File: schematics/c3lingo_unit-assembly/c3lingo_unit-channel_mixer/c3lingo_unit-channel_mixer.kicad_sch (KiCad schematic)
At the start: 83 parts, among them J301 Interconnect, J302 PowerSupply, J303 Output, J304 Inputs, SW301 OnAir_X, SW302 Mute_X, U301 LM833N, U302 LM339, U303 LM339, U304 LM339, U305 LM833N

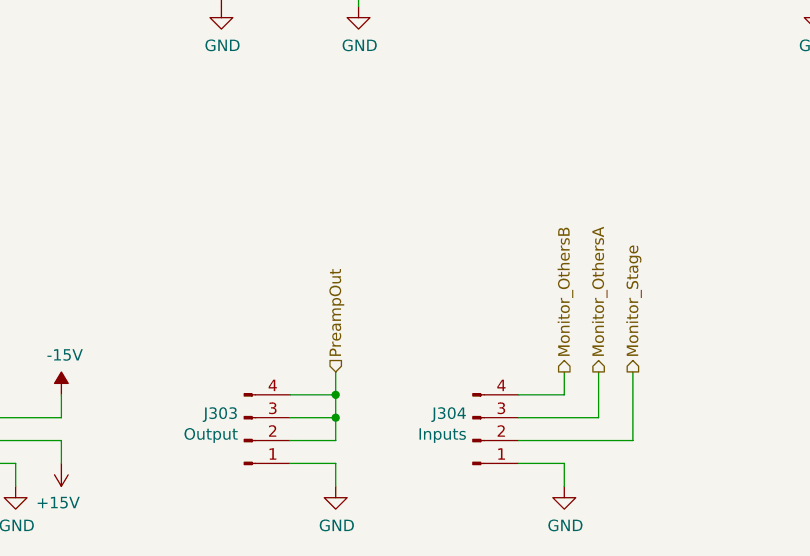
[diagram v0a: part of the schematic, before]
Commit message: Reworks board-to-board connections
Instead of having connections between all boards, use the mix_io board as an audio signal distribution hub.

Note: PCB not updated
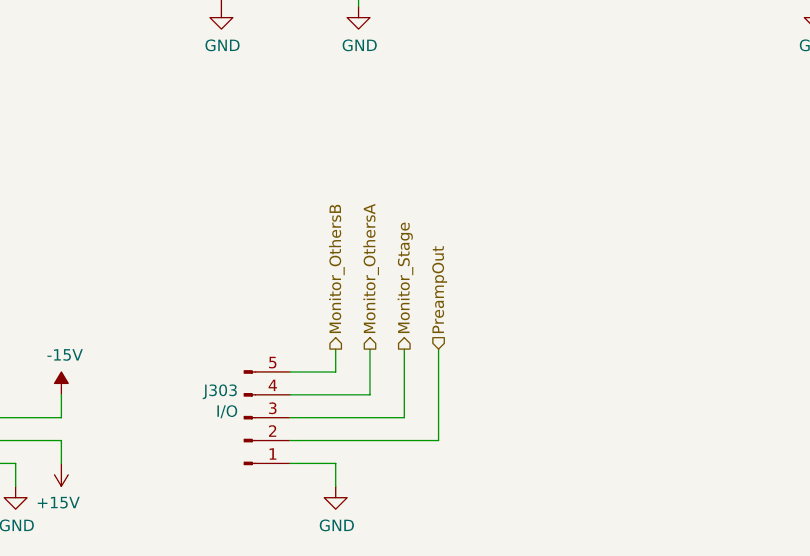
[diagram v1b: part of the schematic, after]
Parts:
- removed J304: Inputs, TerminalBlock_Phoenix:TerminalBlock_Phoenix_PTSM-0,5-4-2.5-H-THR_1x04_P2.50mm_Horizontal, symbol Connector:Conn_01x04_Pin
- J303: value Output -> I/O; footprint TerminalBlock_Phoenix:TerminalBlock_Phoenix_PTSM-0,5-4-2.5-H-THR_1x04_P2.50mm_Horizontal -> TerminalBlock_Phoenix:TerminalBlock_Phoenix_PTSM-0,5-5-2.5-H-THR_1x05_P2.50mm_Horizontal; symbol Connector:Conn_01x04_Pin -> Connector:Conn_01x05_Pin; Model PTSM 0,5/ 4-2,5-H THR -> PTSM 0,5/ 5-2,5-H THR
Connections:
- net Monitor_OthersA: now also J303.4 (Pin_4)
- net Monitor_OthersB: now also J303.5 (Pin_5)
- net Monitor_Stage: now also J303.3 (Pin_3)
- net PreampOut: no longer J303.3 (Pin_3), J303.4 (Pin_4)

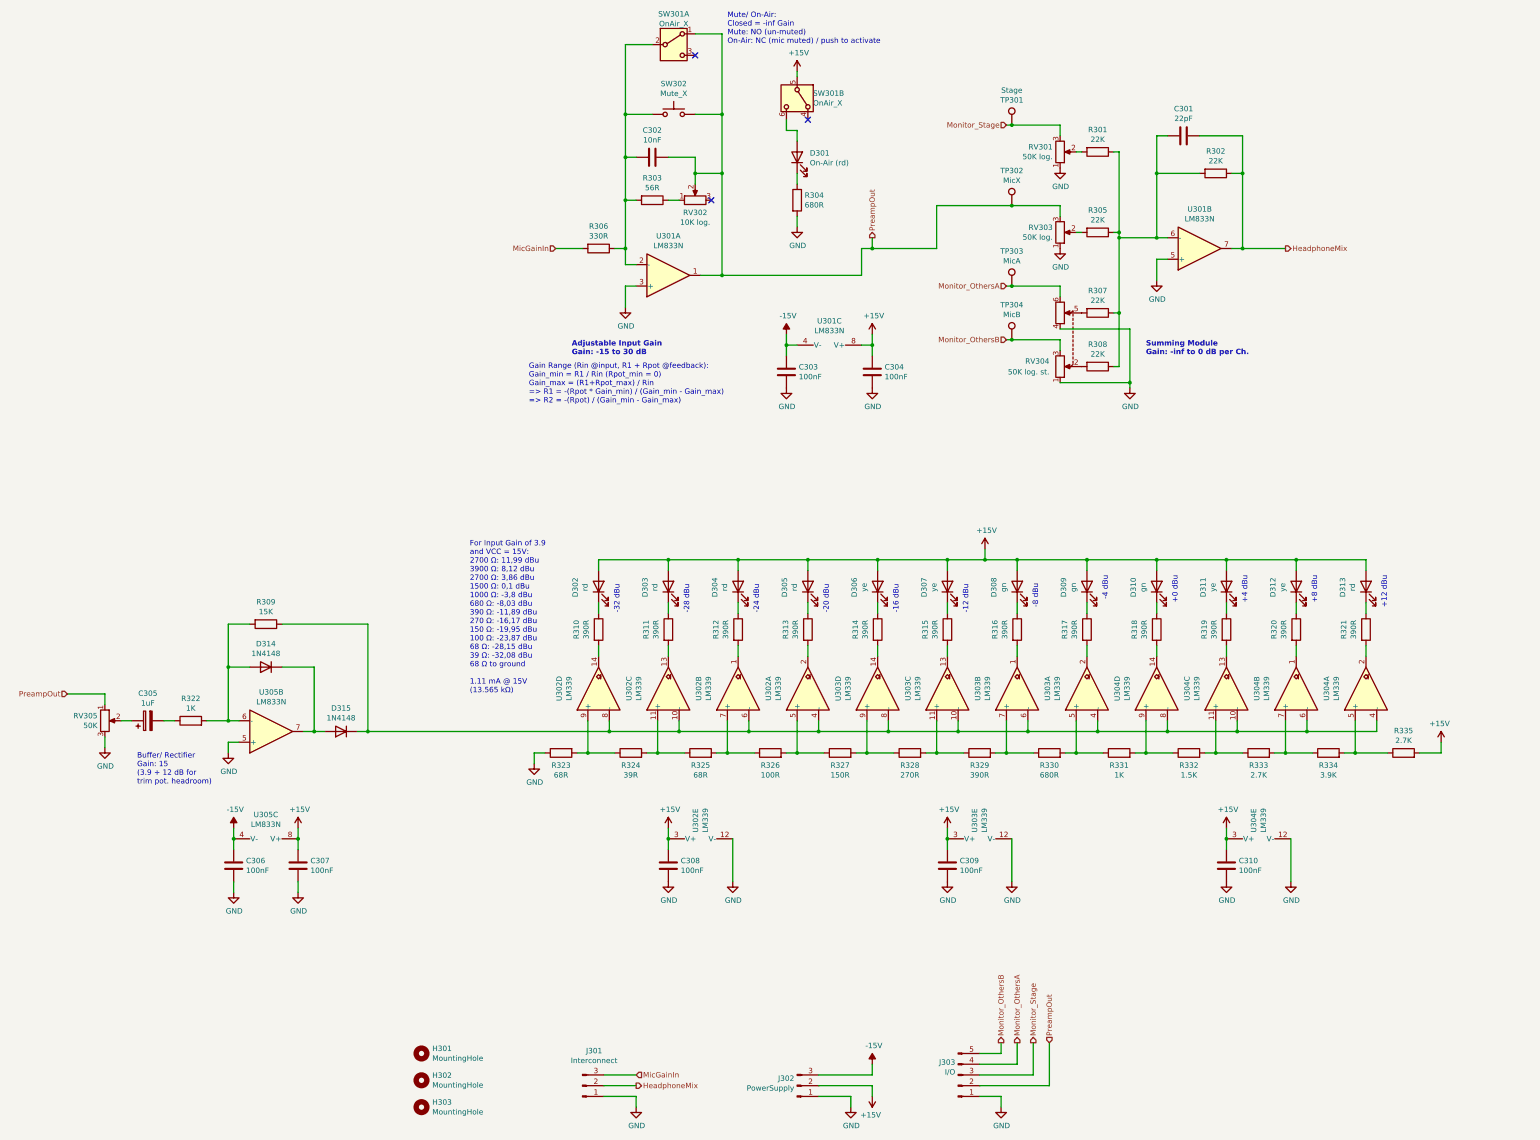
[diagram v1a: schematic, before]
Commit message: Re-layout boards with SMD components
* Channel Mix: Removed vu meter potentiometer as good setting was found (10 dB
  more headroom)
* Channel Mix: Add vu meter alternate power
* Channel I/O: Added jumper for phantom power enable/disable
* Add GND test points
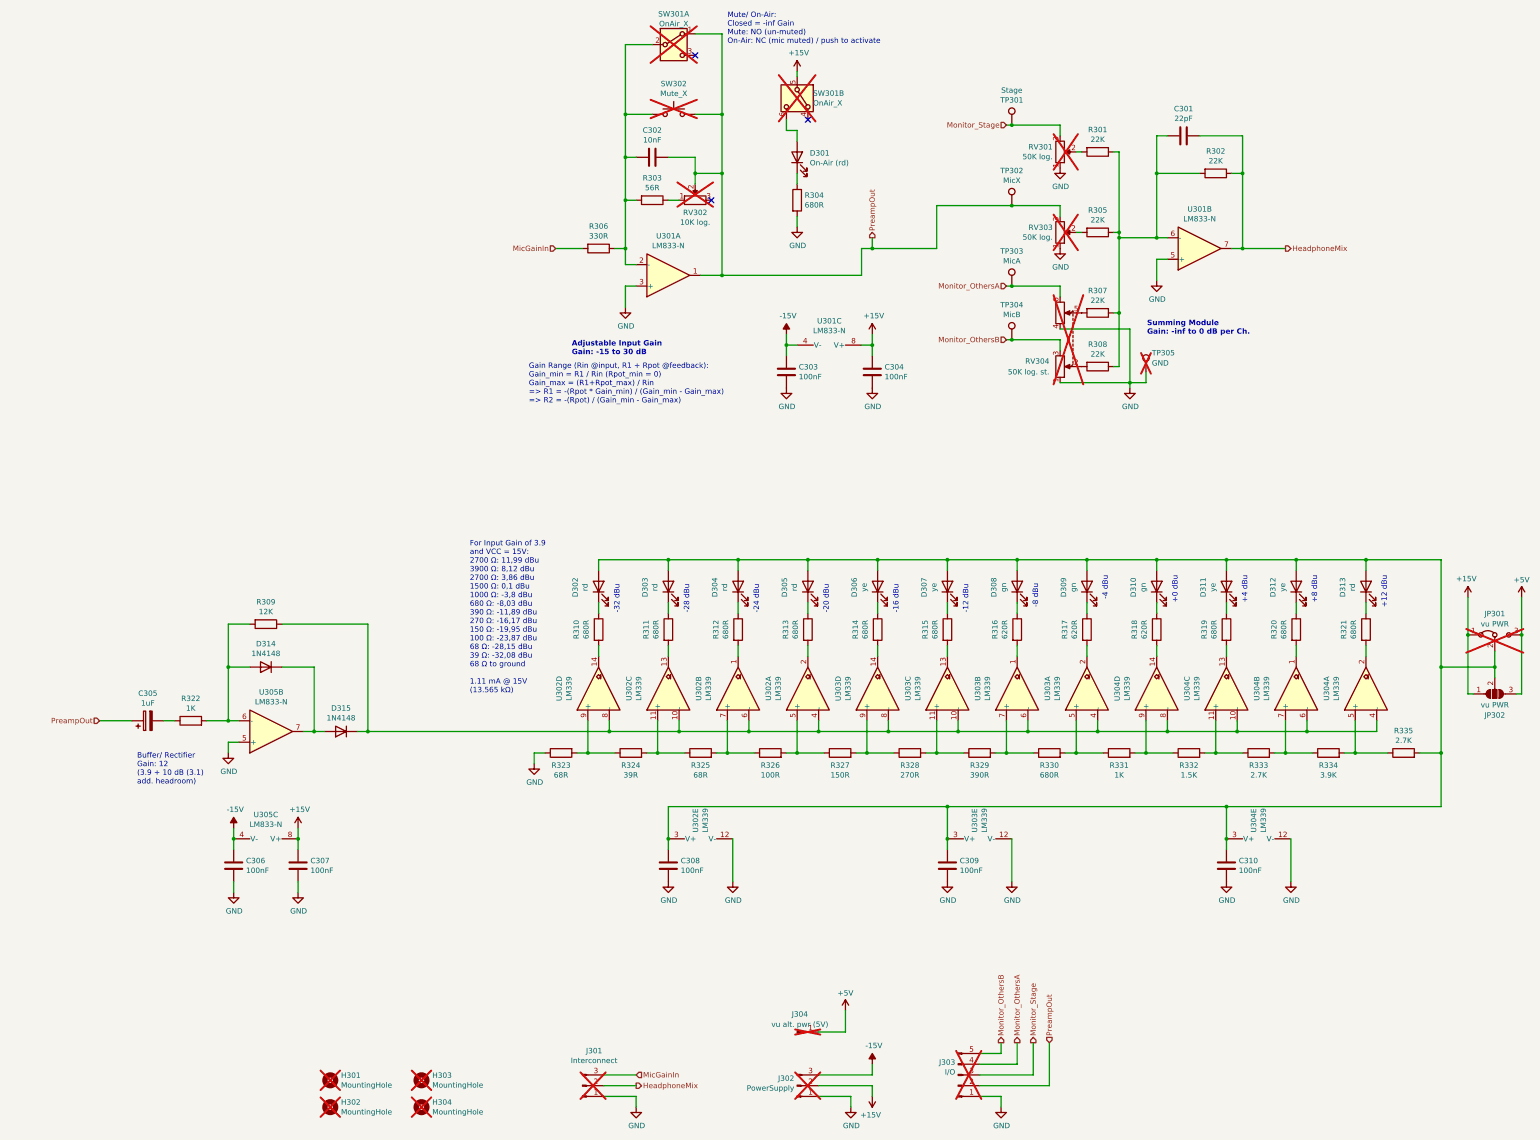
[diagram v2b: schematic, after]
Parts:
- removed RV305: 50K, Potentiometer_THT:Potentiometer_Vishay_T73XX_Horizontal, symbol Device:R_Potentiometer
- added H304: MountingHole, MountingHole:MountingHole_3.2mm_M3, symbol Mechanical:MountingHole
- added J304: vu alt. pwr (5V), Connector_PinHeader_2.54mm:PinHeader_1x01_P2.54mm_Vertical, symbol Connector:Conn_01x01_Pin
- added JP301: vu PWR, Connector_PinHeader_2.54mm:PinHeader_1x03_P2.54mm_Horizontal, symbol Jumper:Jumper_3_Bridged12
- added JP302: vu PWR, Jumper:SolderJumper-3_P1.3mm_Open_RoundedPad1.0x1.5mm_NumberLabels, symbol Jumper:SolderJumper_3_Open
- added TP305: GND, TestPoint:TestPoint_Keystone_5005-5009_Compact, symbol Connector:TestPoint
- C301: footprint Capacitor_THT:C_Disc_D5.0mm_W2.5mm_P5.00mm -> Capacitor_SMD:C_0603_1608Metric_Pad1.08x0.95mm_HandSolder; LCSC Part # (none) -> C1653; Model (none) -> 5% C0G
- C302: footprint Capacitor_THT:C_Disc_D5.0mm_W2.5mm_P5.00mm -> Capacitor_SMD:C_0603_1608Metric_Pad1.08x0.95mm_HandSolder; LCSC Part # (none) -> C57112
- C303, C304, C306, C307, C308, C309, C310: footprint Capacitor_THT:C_Disc_D5.0mm_W2.5mm_P5.00mm -> Capacitor_SMD:C_0603_1608Metric_Pad1.08x0.95mm_HandSolder; LCSC Part # (none) -> C14663; Model (none) -> 10% X7R 25V+
- C305: footprint Capacitor_THT:CP_Radial_D5.0mm_P2.00mm -> Capacitor_SMD:C_Elec_4x5.8; LCSC Part # (none) -> C336256; Model (none) -> 16V low ESR electrolytic
- D301: footprint LED_THT:LED_D5.0mm -> LED_SMD:LED_0603_1608Metric_Pad1.05x0.95mm_HandSolder; Model TLHR5405 -> TODO
- D302, D303, D304, D305, D313: footprint LED_THT:LED_D5.0mm -> LED_SMD:LED_0805_2012Metric_Pad1.15x1.40mm_HandSolder; LCSC Part # (none) -> C84256; Model TLHR5405 -> generic 20 mA, 2.0 V
- D306, D307, D311, D312: footprint LED_THT:LED_D5.0mm -> LED_SMD:LED_0805_2012Metric_Pad1.15x1.40mm_HandSolder; LCSC Part # (none) -> C2296; Model TLHY5405 -> generic 20 mA, 2.1 V
- D308, D309, D310: footprint LED_THT:LED_D5.0mm -> LED_SMD:LED_0805_2012Metric_Pad1.15x1.40mm_HandSolder; LCSC Part # (none) -> C2297; Model TLHG5405 -> generic 20 mA, 2.8-2.9 V
- D314, D315: footprint Diode_THT:D_DO-35_SOD27_P10.16mm_Horizontal -> Diode_SMD:D_SOD-123; LCSC Part # (none) -> C7420318; Model (none) -> 1N4148W (SOD-123)
- H301, H302, H303: now not fitted; now left out of the parts list
- J301, J302, J303, RV301, RV302, RV303, RV304, SW301, SW302: now not fitted
- R301, R302, R305, R307, R308: footprint Resistor_THT:R_Axial_DIN0207_L6.3mm_D2.5mm_P10.16mm_Horizontal -> Resistor_SMD:R_0805_2012Metric_Pad1.20x1.40mm_HandSolder; LCSC Part # (none) -> C17560
- R303, R304, R306, R322, R323, R324, R325, R326, R327, R328, R329, R330, R331, R332, R333, R334, R335: footprint Resistor_THT:R_Axial_DIN0207_L6.3mm_D2.5mm_P10.16mm_Horizontal -> Resistor_SMD:R_0805_2012Metric_Pad1.20x1.40mm_HandSolder
- R309: value 15K -> 12K; footprint Resistor_THT:R_Axial_DIN0207_L6.3mm_D2.5mm_P10.16mm_Horizontal -> Resistor_SMD:R_0805_2012Metric_Pad1.20x1.40mm_HandSolder
- R310, R311, R312, R313, R314, R315, R319, R320, R321: value 390R -> 680R; footprint Resistor_THT:R_Axial_DIN0207_L6.3mm_D2.5mm_P10.16mm_Horizontal -> Resistor_SMD:R_0805_2012Metric_Pad1.20x1.40mm_HandSolder
- R316, R317, R318: value 390R -> 620R; footprint Resistor_THT:R_Axial_DIN0207_L6.3mm_D2.5mm_P10.16mm_Horizontal -> Resistor_SMD:R_0805_2012Metric_Pad1.20x1.40mm_HandSolder
- TP301, TP302, TP303, TP304: now left out of the parts list
- U301, U305: value LM833N -> LM833-N; footprint Package_DIP:DIP-8_W7.62mm_Socket_LongPads -> Package_SO:SOIC-8_3.9x4.9mm_P1.27mm; LCSC Part # (none) -> C473907; Model +DIP-8 Socket -> LM833M or LM833MX (SOIC-8)
- U302, U303, U304: footprint Package_DIP:DIP-14_W7.62mm_Socket_LongPads -> Package_SO:SOIC-14_3.9x8.7mm_P1.27mm; LCSC Part # (none) -> C7948; Model +DIP-14 Socket -> LM339DR (SOIC-14)
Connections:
- net +15V: now also JP301.1 (A), JP302.1 (A); no longer C308.1, C309.1, C310.1, D302.2 (A), D303.2 (A), D304.2 (A), D305.2 (A), D306.2 (A), D307.2 (A), D308.2 (A), D309.2 (A), D310.2 (A), D311.2 (A), D312.2 (A), D313.2 (A), R335.2, U302.3 (V+), U303.3 (V+), U304.3 (V+)
- net GND: now also TP305.1
- net PreampOut: now also C305.1
- new net: C308.1, C309.1, C310.1, D302.2 (A), D303.2 (A), D304.2 (A), D305.2 (A), D306.2 (A), D307.2 (A), D308.2 (A), D309.2 (A), D310.2 (A), D311.2 (A), D312.2 (A), D313.2 (A), JP301.2 (C), JP302.2 (C), R335.2, U302.3 (V+), U303.3 (V+), U304.3 (V+)
- new net +5V: J304.1 (Pin_1), JP301.3 (B), JP302.3 (B)
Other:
- note added: "Buffer/ Rectifier Gain: 12 (3.9 + 10 dB (3.1) add. headroom)"
- note removed: "Buffer/ Rectifier Gain: 15 (3.9 + 12 dB for trim pot. headroom)"

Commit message: Channel-Mix: Rework LED supply voltage
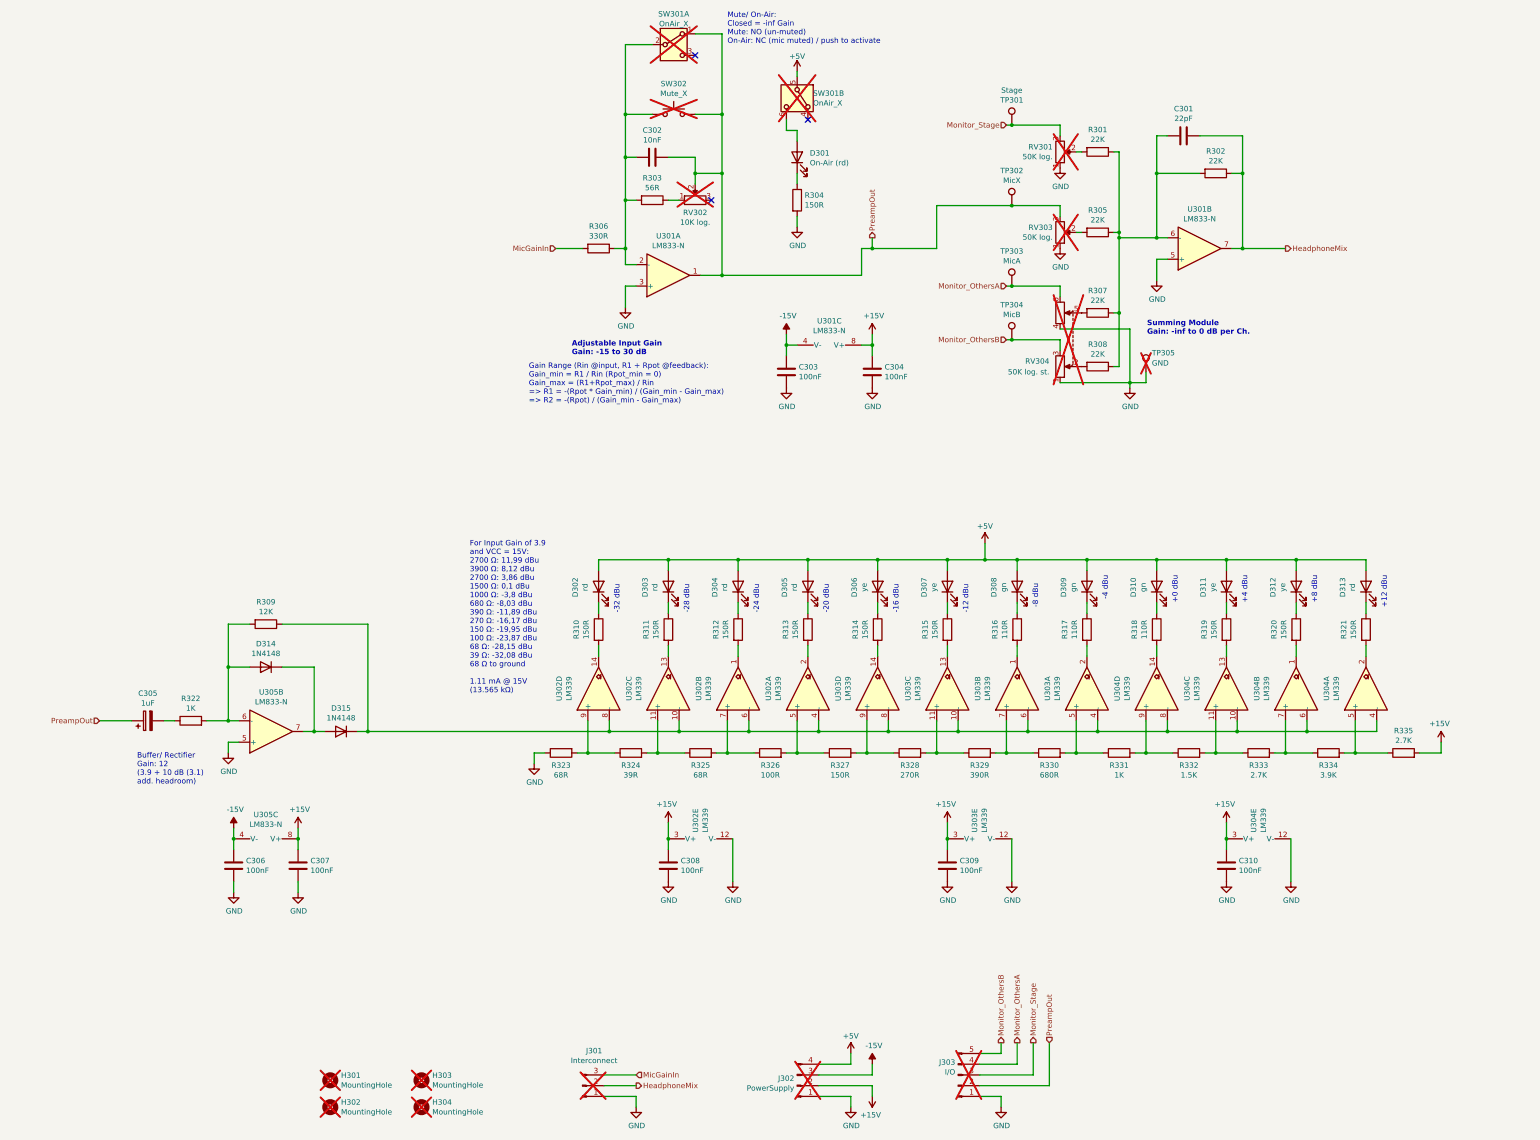
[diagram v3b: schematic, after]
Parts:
- removed J304: vu alt. pwr (5V), Connector_PinHeader_2.54mm:PinHeader_1x01_P2.54mm_Vertical, symbol Connector:Conn_01x01_Pin
- removed JP301: vu PWR, Connector_PinHeader_2.54mm:PinHeader_1x03_P2.54mm_Horizontal, symbol Jumper:Jumper_3_Bridged12
- removed JP302: vu PWR, Jumper:SolderJumper-3_P1.3mm_Open_RoundedPad1.0x1.5mm_NumberLabels, symbol Jumper:SolderJumper_3_Open
- D301: footprint LED_SMD:LED_0603_1608Metric_Pad1.05x0.95mm_HandSolder -> LED_SMD:LED_0805_2012Metric_Pad1.15x1.40mm_HandSolder; LCSC Part # (none) -> C84256; Model TODO -> generic 20 mA, 2.0 V
- J302: footprint TerminalBlock_Phoenix:TerminalBlock_Phoenix_PTSM-0,5-3-2.5-H-THR_1x03_P2.50mm_Horizontal -> TerminalBlock_Phoenix:TerminalBlock_Phoenix_PTSM-0,5-4-2.5-H-THR_1x04_P2.50mm_Horizontal; symbol Connector:Conn_01x03_Pin -> Connector:Conn_01x04_Pin; Model PTSM 0,5/ 3-2,5-H THR -> PTSM 0,5/ 4-2,5-H THR
- R304, R310, R311, R312, R313, R314, R315, R319, R320, R321: value 680R -> 150R
- R316, R317, R318: value 620R -> 110R
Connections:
- net +15V: now also C308.1, C309.1, C310.1, R335.2, U302.3 (V+), U303.3 (V+), U304.3 (V+); no longer SW301.5 (B)
- net +5V: now also D302.2 (A), D303.2 (A), D304.2 (A), D305.2 (A), D306.2 (A), D307.2 (A), D308.2 (A), D309.2 (A), D310.2 (A), D311.2 (A), D312.2 (A), D313.2 (A), J302.4 (Pin_4), SW301.5 (B)

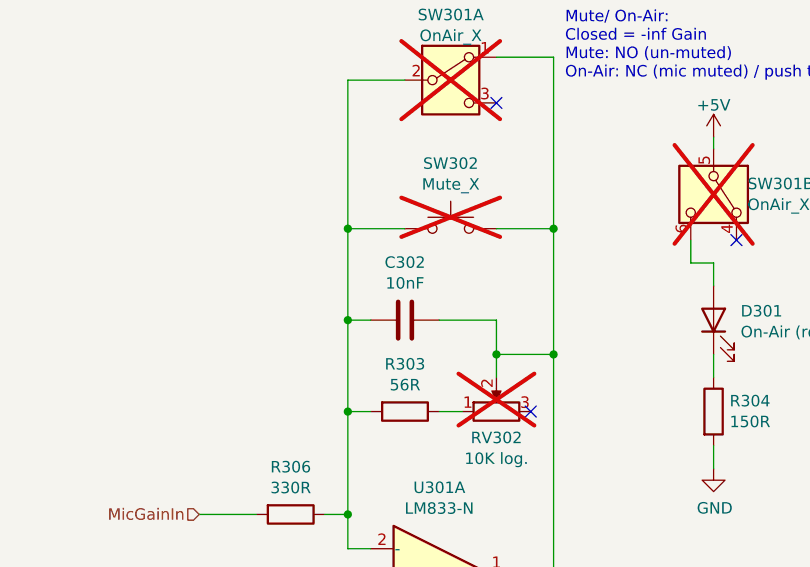
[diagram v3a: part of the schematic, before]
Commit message: Channel Mixer: Fix LP filter at mic gain
1nF has about 15kHz cutoff frequency at full gain
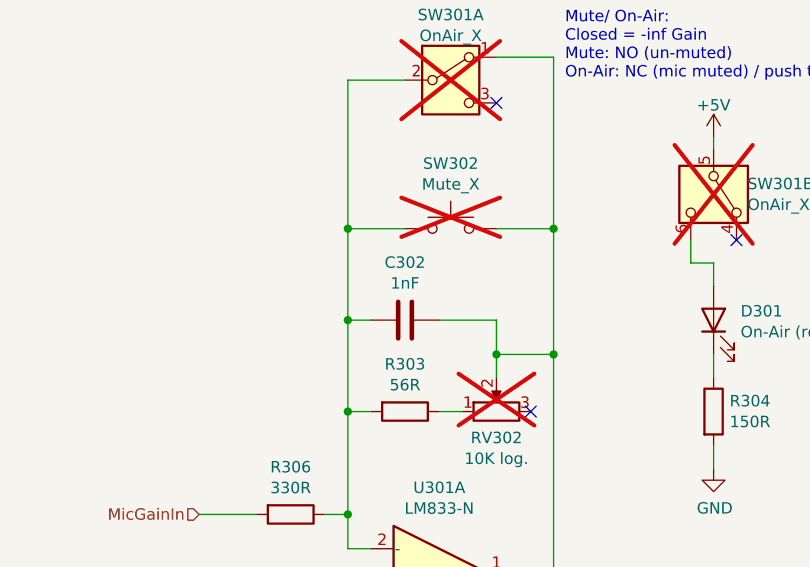
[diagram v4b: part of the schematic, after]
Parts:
- C302: value 10nF -> 1nF; LCSC Part # C57112 -> C1588
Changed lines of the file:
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@@
 	(title_block
 		(title "c3lingo interpeter unit -- channel strip (mixer)")
-		(date "2024-07-07")
-		(rev "v0.3.0")
+		(date "2024-07-08")
+		(rev "v0.3.1")
 		(company "Jannik Beyerstedt (jtbx)")
 		(comment 1 "Prototype 2")
@@
 			)
 		)
-		(property "Value" "10nF"
+		(property "Value" "1nF"
 			(at 168.91 50.5206 90)
 			(effects
@@
 			)
 		)
-		(property "LCSC Part #" "C57112"
+		(property "LCSC Part #" "C1588"
 			(at 168.91 54.61 0)
 			(effects
